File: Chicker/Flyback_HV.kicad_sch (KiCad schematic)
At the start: 64 parts, among them Q2 IRFR3410TRPBF, Q3 FGH50T65SQD-F155, Q5 TN2130K1-G, Q6 IPD60R3K4CEAUMA1, Q7 FGH50T65SQD-F155, Q8 TN2130K1-G, T1 DA2034, U2 LT3750, U4 MCP14A0454-E/SN

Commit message: chicker updates
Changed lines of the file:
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@@
     (effects (font (size 1.27 1.27)) (justify right))
+  )
+  (hierarchical_label "HV" (shape input) (at 215.9 31.75 0) (fields_autoplaced)
+    (effects (font (size 1.27 1.27)) (justify left))
   )
   (hierarchical_label "CHICKER_HV" (shape input) (at 151.13 111.76 0) (fields_autoplaced)

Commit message: chicker v1.1 updates
nearly done, need to fix rules
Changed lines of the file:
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@@
   (junction (at 62.23 58.42) (diameter 0) (color 0 0 0 0)
   )
-  (junction (at 124.46 104.14) (diameter 0) (color 0 0 0 0)
-  )
   (junction (at 121.92 182.88) (diameter 0) (color 0 0 0 0)
   )
@@
   (junction (at 76.2 83.82) (diameter 0) (color 0 0 0 0)
   )
-  (junction (at 121.92 153.67) (diameter 0) (color 0 0 0 0)
-  )
   (junction (at 133.35 41.91) (diameter 0) (color 0 0 0 0)
   )
@@
   )
   (junction (at 36.83 123.19) (diameter 0) (color 0 0 0 0)
+  )
+  (junction (at 215.9 31.75) (diameter 0) (color 0 0 0 0)
   )
   (junction (at 124.46 111.76) (diameter 0) (color 0 0 0 0)
@@
     (stroke (width 0) (type default))
   )
+  (wire (pts (xy 215.9 31.75) (xy 220.98 31.75))
+    (stroke (width 0) (type default))
+  )
   (wire (pts (xy 229.87 93.98) (xy 246.38 93.98))
     (stroke (width 0) (type default))
@@
     (stroke (width 0) (type default))
   )
+  (wire (pts (xy 215.9 31.75) (xy 215.9 33.02))
+    (stroke (width 0) (type default))
+  )
   (wire (pts (xy 87.63 172.72) (xy 87.63 173.99))
     (stroke (width 0) (type default))
@@
     (stroke (width 0) (type default))
   )
-  (wire (pts (xy 151.13 104.14) (xy 124.46 104.14))
-    (stroke (width 0) (type default))
-  )
   (wire (pts (xy 60.96 123.19) (xy 63.5 123.19))
     (stroke (width 0) (type default))
@@
     (stroke (width 0) (type default))
   )
-  (wire (pts (xy 215.9 33.02) (xy 215.9 31.75))
-    (stroke (width 0) (type default))
-  )
   (wire (pts (xy 90.17 123.19) (xy 90.17 124.46))
     (stroke (width 0) (type default))
@@
   )
   (wire (pts (xy 128.27 41.91) (xy 133.35 41.91))
-    (stroke (width 0) (type default))
-  )
-  (wire (pts (xy 148.59 153.67) (xy 121.92 153.67))
     (stroke (width 0) (type default))
   )
@@
     (effects (font (size 1.27 1.27)) (justify left bottom))
   )
-  (label "HV" (at 215.9 31.75 0) (fields_autoplaced)
+  (label "HV" (at 212.09 31.75 0) (fields_autoplaced)
     (effects (font (size 1.27 1.27)) (justify left bottom))
   )
@@
     (effects (font (size 1.27 1.27)) (justify right))
   )
-  (hierarchical_label "HV" (shape input) (at 151.13 104.14 0) (fields_autoplaced)
-    (effects (font (size 1.27 1.27)) (justify left))
-  )
-  (hierarchical_label "HV" (shape input) (at 148.59 153.67 0) (fields_autoplaced)
-    (effects (font (size 1.27 1.27)) (justify left))
-  )
   (hierarchical_label "CHARGE" (shape input) (at 49.53 63.5 180) (fields_autoplaced)
     (effects (font (size 1.27 1.27)) (justify right))
@@
     (effects (font (size 1.27 1.27)) (justify right))
   )
-  (hierarchical_label "HV" (shape input) (at 215.9 31.75 0) (fields_autoplaced)
+  (hierarchical_label "HV" (shape input) (at 220.98 31.75 0) (fields_autoplaced)
     (effects (font (size 1.27 1.27)) (justify left))
   )

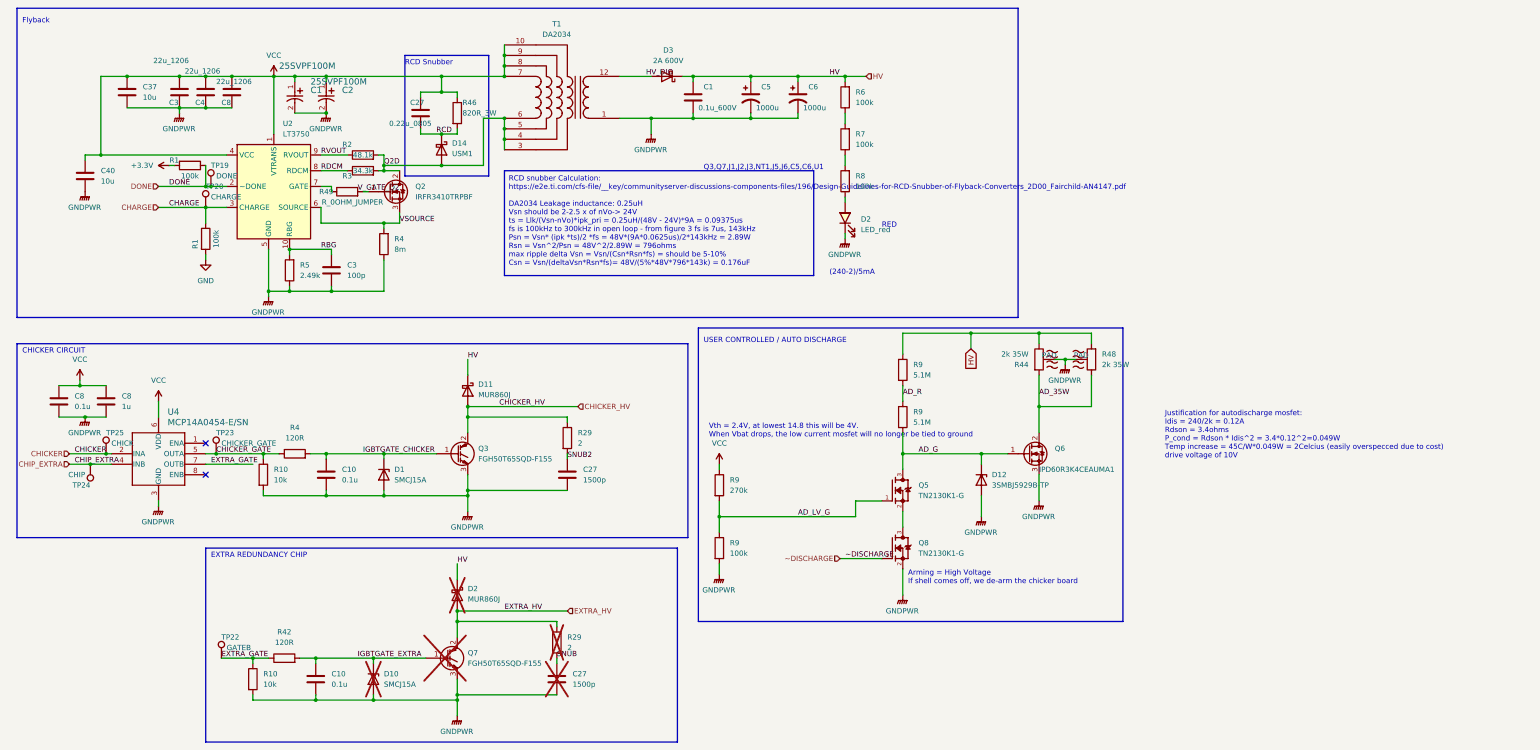
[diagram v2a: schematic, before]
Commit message: v1.1 mostly done, need to add tooling holes
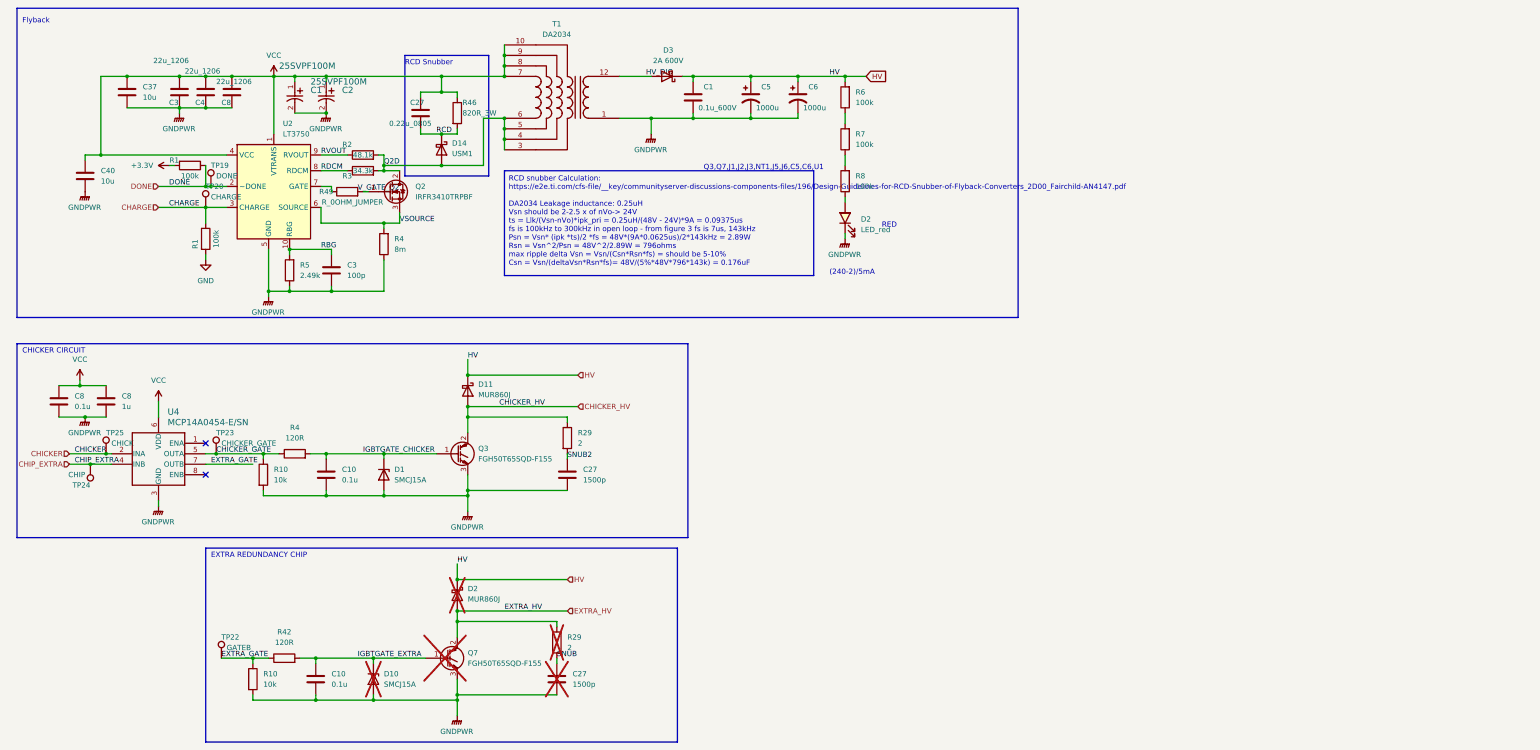
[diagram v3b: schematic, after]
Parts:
- removed D12: 3SMBJ5929B-TP, bots:D_SMB, symbol bots:D_ZENER_3SMBJ5929B-TP
- removed Q5, Q8: TN2130K1-G, bots:SOT95P240X111-3N, symbol bots:TN2130K1-G
- removed Q6: IPD60R3K4CEAUMA1, bots:DPAK-3_ONS, symbol bots:IPD60R3K4CEAUMA1
- removed R44, R48: 2k 35W, bots:TO-220-2_Horizontal_TabDown, symbol bots:2k_35W
- removed R9: 100k, bots:R_0603_1608Metric, symbol bots:R_100k
- removed R9: 270k, bots:R_0603_1608Metric, symbol bots:R_270k
- removed R9 (x2): 5.1M, bots:R_0603_1608Metric, symbol bots:R_5.1M
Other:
- note removed: "Arming = High Voltage If shell comes off, we de-arm the chicker board"
- note removed: "Justification for autodischarge mosfet: Idis = 240/2k = 0.12A Rdson = 3.4ohms P_cond = Rdson * Idis^2 = 3.4*0.12^2=0.049W Temp increase = 45C/W*0.049W = 2Celcius (easily overspecced due to cost) drive voltage of 10V"
- note removed: "USER CONTROLLED / AUTO DISCHARGE"
- note removed: "Vth = 2.4V, at lowest 14.8 this will be 4V. When Vbat drops, the low current mosfet will no longer be tied to ground"

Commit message: chicker modifications (mostly ready to order)
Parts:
- removed TP23: CHICKER_GATE, bots:TestPoint_Pad_1.0x1.0mm, symbol bots:TestPoint_1x1
- added R14, R57: 0R, bots:R_0402_1005Metric, symbol thebots_symlib:R_0R_0402
- added TP14: K_GATE, bots:TestPoint_Pad_1.0x1.0mm, symbol bots:TestPoint_1x1
- TP22: value GATEB -> C_GATE
- renumbered C27 to C10, C1 to C28, C8 to C34, C8 to C35, C10 to C38, C27 to C39, C3 to C7, C10 to C9, D2 to D4, R7 to R10, R10 to R2, R1 to R27, R8 to R29, R5 to R3, R10 to R41, R29 to R43, R2 to R5, R3 to R6, R4 to R7, R29 to R8, R6 to R9, U4 to U2, U2 to U4
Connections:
- net CHICKER renamed CHIP_0R
- net CHIP_0R: now also R57.2
- net CHICKER_GATE renamed KICK_GATE
- net KICK_GATE: now also TP14.1
- net CHICKER_HV renamed KICK_HV
- net CHIP_EXTRA renamed KICK_0R
- net KICK_0R: now also R14.2
- net EXTRA_GATE renamed CHIP_GATE
- net EXTRA_HV renamed CHIP_HV
- net IGBTGATE_CHICKER renamed IGBTGATE_KICK
- net IGBTGATE_EXTRA renamed IGBTGATE_CHIP
- new net CHIP: R57.1
- new net KICK: R14.1
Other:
- moved on the sheet: C10, C9, D1, D11, Q3, R2, R4, R8

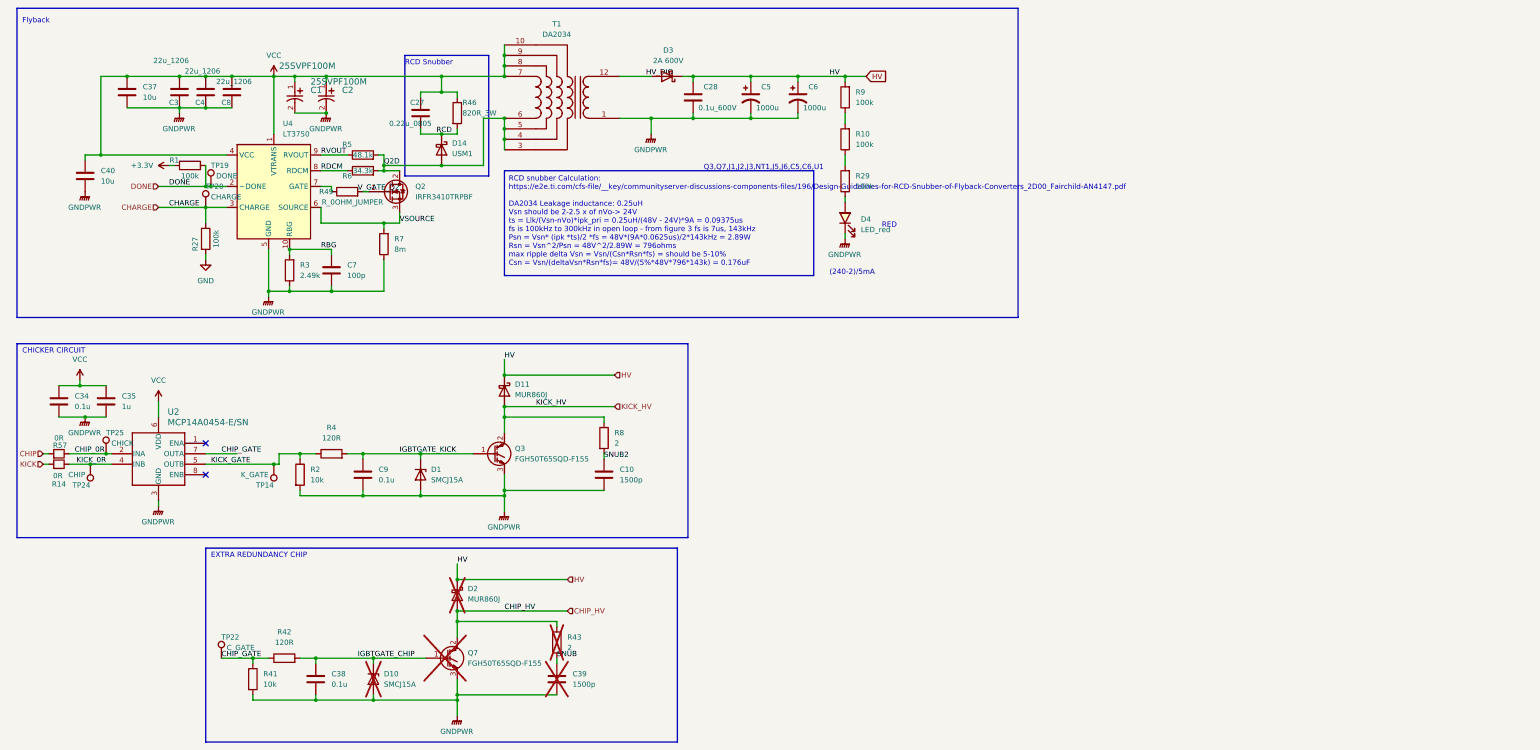
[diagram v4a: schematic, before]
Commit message: ESD+schematic fixes
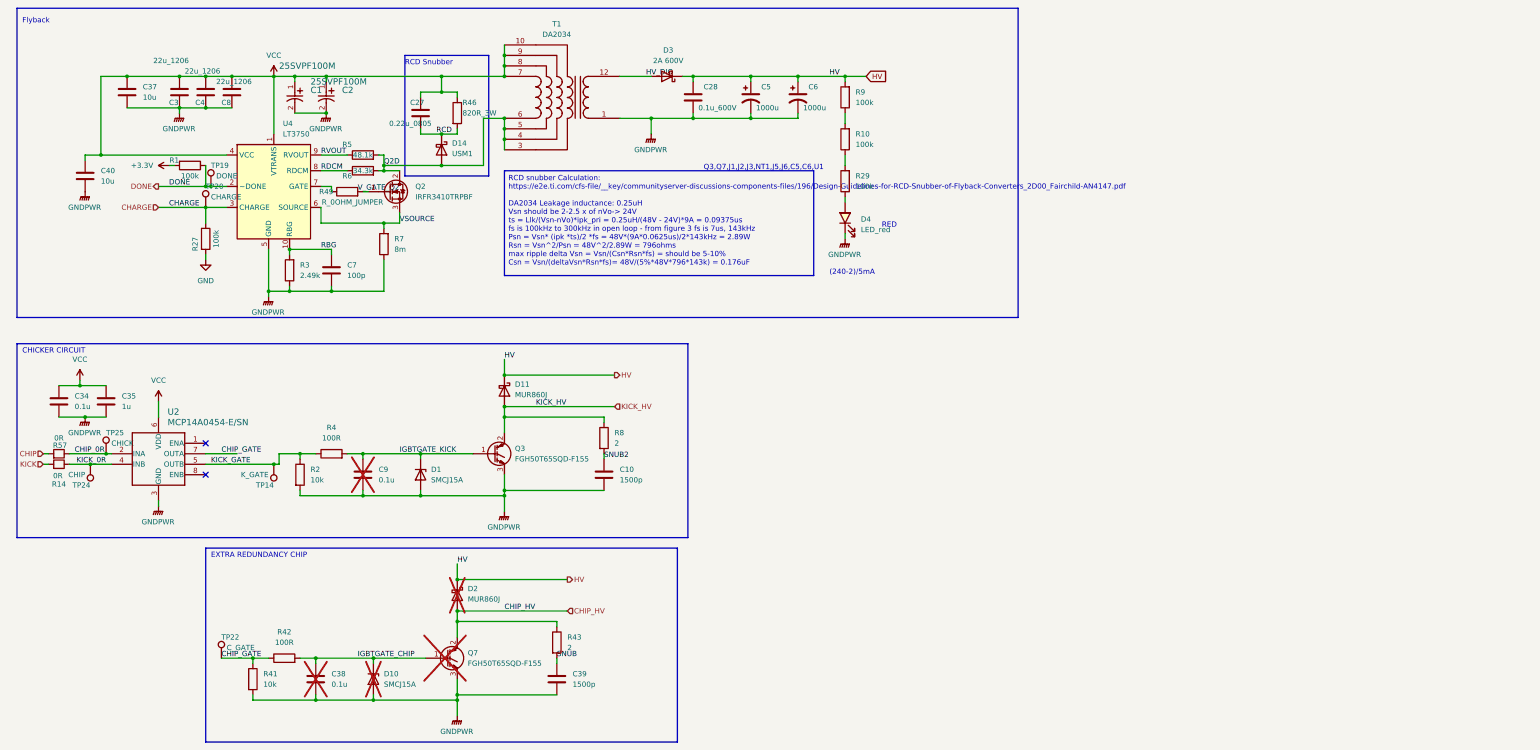
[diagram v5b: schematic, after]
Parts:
- removed R4, R42: 120R, bots:R_0603_1608Metric, symbol bots:R_120R
- added R4, R42: 100R, bots:R_0603_1608Metric, symbol bots:R_100R
- C38, C9: now not fitted; now left out of the parts list
- C39, R43: now fitted; now in the parts list
- Q3, Q7: value FGH50T65SQD-F155 -> FGH50T65SQD-F155
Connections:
- net CHIP_GATE: now also R42.1
- net IGBTGATE_CHIP: now also R42.2
- net IGBTGATE_KICK: now also R4.2
- net KICK_GATE: now also R4.1

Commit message: chicker v1.1 basic parts
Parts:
- removed C1, C2: 25SVPF100M, bots:CAP_25SVPF100M, symbol bots:25SVPF100M
- removed C27: 0.22u_0805, bots:C_0805_2012Metric, symbol bots:C_0.22u_0805
- removed R3: 2.49k, bots:R_0603_1608Metric, symbol bots:R_2.49k
- removed R5: 48.1k, bots:R_0603_1608Metric, symbol bots:R_47.5k
- removed R6: 34.3k, bots:R_0603_1608Metric, symbol bots:R_34k
- added C1, C2: 25SVPF100M_alternate, bots:CAP_25SVPF100M, symbol bots:25SVPF100M_alternate
- added C27: 0.1u, bots:C_0603_1608Metric, symbol bots:C_0.1u
- added R3: 2.4k, bots:R_0603_1608Metric, symbol bots:R_2.4k
- added R5: 40.2k, bots:R_0603_1608Metric, symbol bots:R_40.2k
- added R6: 33k, bots:R_0603_1608Metric, symbol bots:R_33k
- R46: now left out of the parts list
- R7: JLC Extended (none) -> yes; LCSC C326567 -> C7420012; MPN PE1206FRF470R008L -> FRM121WFR008TM; Manufacturer YAGEO -> FOJAN; Price 0.0695 -> 0.0422
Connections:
- net GNDPWR: now also C1.2, C2.2, R3.2
- net Q2D: now also R5.2, R6.2
- net RBG: now also R3.1
- net RCD: now also C27.2
- net RDCM: now also R6.1
- net RVOUT: now also R5.1
- net VCC: now also C1.1, C2.1, C27.1
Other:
- note added: "1.24*40.2/2.4*10 -1.25= 206V ish (good)"

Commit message: more parts
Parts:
- removed D3: 2A 600V, bots:D_SMB, symbol bots:MURS160-E3/52T
- removed R4, R42: 100R, bots:R_0603_1608Metric, symbol bots:R_100R
- added D3: MURS160-E3/52T_alternate, bots:D_SMB, symbol bots:D_MURS160-E3/52T_alternate
- added R4, R42: 75R, bots:R_0603_1608Metric, symbol bots:R_75R
- C10, C39: LCSC C342996 -> C1717; MPN C2012C0G2A152JT000N -> 0805B152K500NT; Manufacturer TDK -> FH (Guangdong Fenghua Advanced Tech); Price 0.0396 -> 0.066
- R43, R8: JLC Extended (none) -> no
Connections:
- net CHIP_GATE: now also R42.1
- net HV: now also D3.1 (K)
- net HV_DIO: now also D3.2 (A)
- net IGBTGATE_CHIP: now also R42.2
- net IGBTGATE_KICK: now also R4.2
- net KICK_GATE: now also R4.1
